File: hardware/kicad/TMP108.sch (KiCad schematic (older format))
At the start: 33 parts, among them J1 Screw_Terminal_01x08, J2 Screw_Terminal_01x08, J3 CAN, SW1 PRG, SW2 SCR, SW3 PRG-VALUE, U1 Teensy_3.2, U2 TMR-1211, U3 MCP2551-I-P

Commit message: Add smoothing capacitor to PSU
1000uF capacitor across 5V output to manage instability in ADC reference voltage.
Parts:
- added C5: 1000uF, Capacitor_THT:CP_Radial_D8.0mm_P5.00mm, symbol Device:CP
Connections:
- net +5V: now also C5.1
- net GND: now also C5.2
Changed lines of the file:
@@
 $EndComp
 Wire Wire Line
-	7900 3500 8200 3500
-Wire Wire Line
-	7900 3100 8200 3100
+	7900 3100 8000 3100
 Connection ~ 9350 3100
 Wire Wire Line
@@
 Wire Wire Line
 	900  4100 900  4550
+$Comp
+L Device:CP C5
+U 1 1 629FD333
+P 8000 3300
+F 0 "C5" H 8118 3346 50  0000 L CNN
+F 1 "1000uF" H 8000 3200 50  0000 L CNN
+F 2 "Capacitor_THT:CP_Radial_D8.0mm_P5.00mm" H 8038 3150 50  0001 C CNN
+F 3 "~" H 8000 3300 50  0001 C CNN
+	1    8000 3300
+	1    0    0    -1
+$EndComp
+Connection ~ 8000 3100
+Wire Wire Line
+	7900 3500 8000 3500
+Wire Wire Line
+	8000 3150 8000 3100
+Wire Wire Line
+	8000 3100 8200 3100
+Wire Wire Line
+	8000 3450 8000 3500
+Connection ~ 8000 3500
+Wire Wire Line
+	8000 3500 8200 3500
 $EndSCHEMATC

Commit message: Add CAN terminator
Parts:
- removed C3, C4: 560p, Capacitor_THT:C_Rect_L4.6mm_W3.0mm_P2.50mm_MKS02_FKP02, symbol Device:C
- removed R14: 100R, Resistor_THT:R_Axial_DIN0207_L6.3mm_D2.5mm_P7.62mm_Horizontal, symbol Device:R
- removed SW2: SCR, Button_Switch_THT:SW_DIP_SPSTx01_Slide_6.7x4.1mm_W7.62mm_P2.54mm_LowProfile, symbol Switch:SW_DIP_x01
- added SW2: BUS, Package_DIP:DIP-4_W7.62mm_LongPads, symbol Switch:SW_DIP_x02
- R13: value 100R -> 120R
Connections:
- net CAN_L: now also SW2.4
- net CAN_SCR: now also SW2.3
- net GND: now also SW2.2
- net TERM_A: now reaches R13.2
- net TERM_A: now also SW2.1
- no-connect marks 4 -> 7
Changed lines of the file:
@@
-$EndComp
-$Comp
-L Device:R R14
-U 1 1 5F21EFF3
-P 9000 4700
-F 0 "R14" H 8950 4700 50  0000 R CNN
-F 1 "100R" V 9000 4700 39  0000 C CNN
-F 2 "Resistor_THT:R_Axial_DIN0207_L6.3mm_D2.5mm_P7.62mm_Horizontal" V 8930 4700 50  0001 C CNN
-F 3 "~" H 9000 4700 50  0001 C CNN
-	1    9000 4700
-	-1   0    0    1
-$EndComp
-$Comp
-L Device:R R13
-U 1 1 5F21F397
-P 8750 4700
-F 0 "R13" H 8950 4700 50  0000 R CNN
-F 1 "100R" V 8750 4700 39  0000 C CNN
-F 2 "Resistor_THT:R_Axial_DIN0207_L6.3mm_D2.5mm_P7.62mm_Horizontal" V 8680 4700 50  0001 C CNN
-F 3 "~" H 8750 4700 50  0001 C CNN
-	1    8750 4700
-	1    0    0    -1
-$EndComp
-$Comp
-L Device:C C4
-U 1 1 5F233FC6
-P 9000 5000
-F 0 "C4" H 8900 5000 50  0000 R CNN
-F 1 "560p" H 9000 5100 39  0000 R CNN
-F 2 "Capacitor_THT:C_Rect_L4.6mm_W3.0mm_P2.50mm_MKS02_FKP02" H 9038 4850 50  0001 C CNN
-F 3 "~" H 9000 5000 50  0001 C CNN
-	1    9000 5000
-	-1   0    0    1
-$EndComp
-$Comp
-L Device:C C3
-U 1 1 5F2499AC
-P 8750 5000
-F 0 "C3" H 8850 5000 50  0000 L CNN
-F 1 "560p" H 8750 5100 39  0000 R CNN
-F 2 "Capacitor_THT:C_Rect_L4.6mm_W3.0mm_P2.50mm_MKS02_FKP02" H 8788 4850 50  0001 C CNN
-F 3 "~" H 8750 5000 50  0001 C CNN
-	1    8750 5000
-	-1   0    0    1
 $EndComp
 $Comp
@@
 NoConn ~ 4850 2800
 Wire Wire Line
-	8650 4300 8750 4300
-Wire Wire Line
-	8650 4500 9000 4500
-Wire Wire Line
-	8750 4550 8750 4300
-Wire Wire Line
-	9000 4550 9000 4500
-Wire Wire Line
 	7550 5150 8150 5150
 Connection ~ 7550 5150
-Wire Wire Line
-	8750 5150 9000 5150
-Connection ~ 8750 5150
 Wire Wire Line
 	7650 4600 7550 4600
@@
 	8150 4800 8150 5150
 Connection ~ 8150 4800
-Connection ~ 8150 5150
-Wire Wire Line
-	8150 5150 8750 5150
 NoConn ~ 7650 4500
 Text Label 1500 4100 0    50   ~ 0
@@
 Text Notes 10000 3800 2    50   ~ 10
 CAN INTERFACE
-Connection ~ 8750 4300
-Wire Wire Line
-	8750 4300 10200 4300
-Connection ~ 9000 4500
-Wire Wire Line
-	9000 4500 10300 4500
 Wire Notes Line
 	9100 2050 10450 2050
@@
 Text Label 4850 2700 2    50   ~ 0
 LED_PWR
-Text Label 10000 4950 2    50   ~ 0
+Text Label 10000 4950 0    50   ~ 0
 CAN_SCR
 Wire Wire Line
@@
 ADDR_7
 $Comp
-L Switch:SW_DIP_x01 SW2
-U 1 1 60541E2C
-P 1200 4100
-F 0 "SW2" H 1200 4250 50  0000 C CNN
-F 1 "SCR" H 1200 3950 50  0000 C CNN
-F 2 "Button_Switch_THT:SW_DIP_SPSTx01_Slide_6.7x4.1mm_W7.62mm_P2.54mm_LowProfile" H 1200 4100 50  0001 C CNN
-F 3 "~" H 1200 4100 50  0001 C CNN
-	1    1200 4100
-	1    0    0    -1
-$EndComp
-$Comp
 L Device:R R10
 U 1 1 6057CA79
@@
 U 1 1 60F2AB82
 P 5950 3000
-F 0 "U1" H 6500 1433 50  0000 C CNN
-F 1 "Teensy_3.2" H 6500 1524 50  0000 C CNN
+F 0 "U1" H 6100 1450 50  0000 C CNN
+F 1 "Teensy_3.2" H 6250 1550 50  0000 C CNN
 F 2 "Package_DIP:DIP-28_W15.24mm_LongPads" H 5950 3000 50  0001 C CNN
 F 3 "" H 5950 3000 50  0001 C CNN
@@
 Wire Wire Line
 	9750 3100 10400 3100
-Wire Wire Line
-	900  4100 900  4550
 $Comp
 L Device:CP C5
@@
 Wire Wire Line
 	8000 3500 8200 3500
+NoConn ~ 5400 1500
+NoConn ~ 5300 1500
+NoConn ~ 5200 1500
+$Comp
+L Device:R R13
+U 1 1 62A3BFE8
+P 9500 4650
+F 0 "R13" V 9400 4700 50  0000 R CNN
+F 1 "120R" V 9500 4650 39  0000 C CNN
+F 2 "Resistor_THT:R_Axial_DIN0207_L6.3mm_D2.5mm_P7.62mm_Horizontal" V 9430 4650 50  0001 C CNN
+F 3 "~" H 9500 4650 50  0001 C CNN
+	1    9500 4650
+	0    -1   -1   0
+$EndComp
+$Comp
+L Switch:SW_DIP_x02 SW2
+U 1 1 62A67242
+P 1200 4100
+F 0 "SW2" H 1200 4350 50  0000 C CNN
+F 1 "BUS" H 1200 3950 50  0000 C CNN
+F 2 "Package_DIP:DIP-4_W7.62mm_LongPads" H 1200 4100 50  0001 C CNN
+F 3 "~" H 1200 4100 50  0001 C CNN
+	1    1200 4100
+	1    0    0    -1
+$EndComp
+Wire Wire Line
+	900  4100 900  4550
+Text Label 10000 4650 0    50   ~ 0
+TERM_A
+Wire Wire Line
+	10000 4650 9650 4650
+Text Label 10000 4800 0    50   ~ 0
+TERM_B
+Wire Wire Line
+	8650 4300 9250 4300
+Wire Wire Line
+	9350 4650 9250 4650
+Wire Wire Line
+	9250 4650 9250 4300
+Connection ~ 9250 4300
+Wire Wire Line
+	9250 4300 10200 4300
+Wire Wire Line
+	10000 4800 9050 4800
+Wire Wire Line
+	9050 4800 9050 4500
+Connection ~ 9050 4500
+Wire Wire Line
+	9050 4500 10300 4500
+Wire Wire Line
+	8650 4500 9050 4500
+Text Label 900  4000 2    50   ~ 0
+TERM_A
+Text Label 1500 4000 0    50   ~ 0
+TERM_B
 $EndSCHEMATC

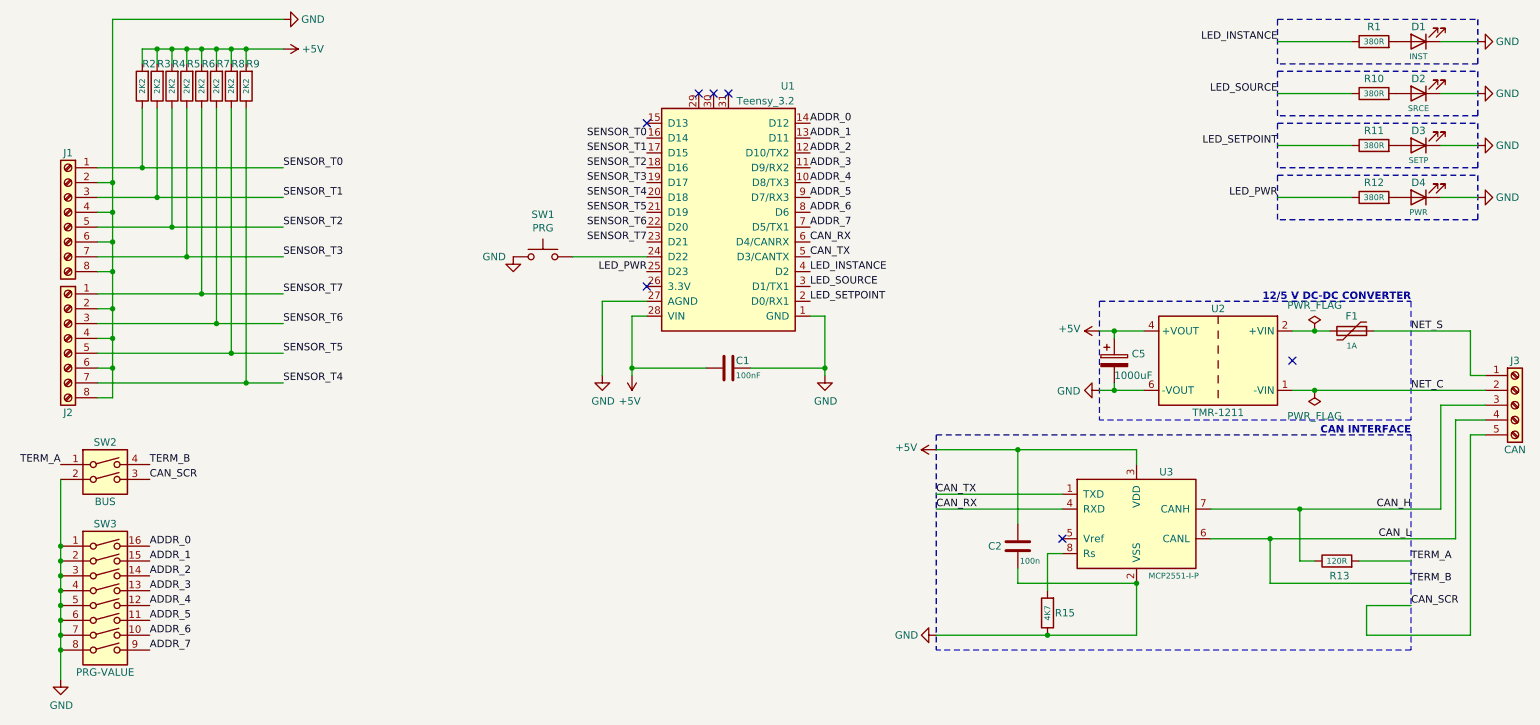
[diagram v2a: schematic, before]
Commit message: Add LED for transmit interval
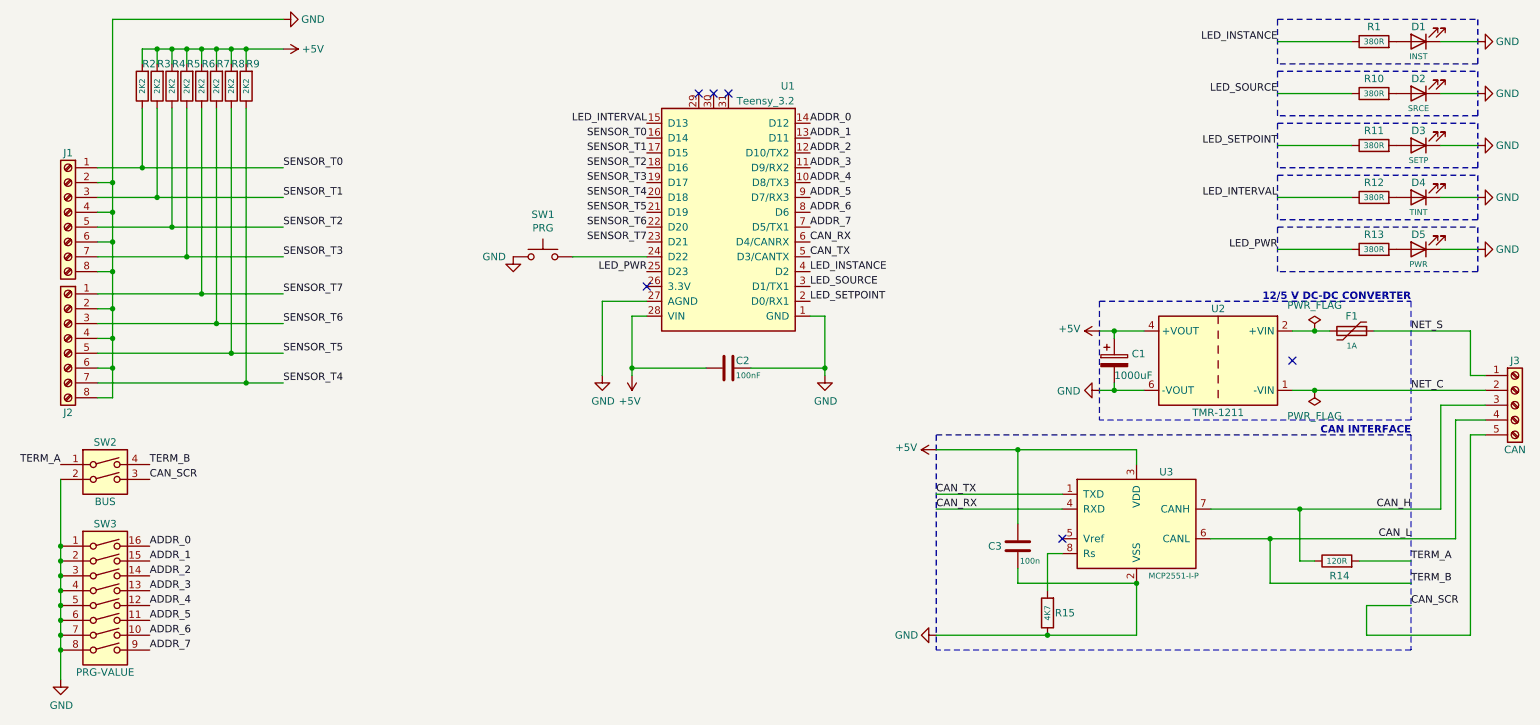
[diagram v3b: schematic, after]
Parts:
- added D4: TINT, LED_THT:LED_D1.8mm_W3.3mm_H2.4mm, symbol Device:LED
- added R12: 380R, Resistor_THT:R_Axial_DIN0207_L6.3mm_D2.5mm_P7.62mm_Horizontal, symbol Device:R
- renumbered C5 to C1, C1 to C2, C2 to C3, D4 to D5, R12 to R13, R13 to R14
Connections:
- net GND: now also D4.1 (K)
- net LED_INTERVAL: now reaches U1.15 (D13)
- net LED_INTERVAL: now also R12.1
- new net: D4.2 (A), R12.2
- no-connect marks 7 -> 6
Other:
- moved on the sheet: D5, R13
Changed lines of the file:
@@
 $EndComp
 $Comp
-L Device:R R12
+L Device:R R13
 U 1 1 5F2B75CF
-P 9750 2200
-F 0 "R12" V 9850 2200 50  0000 C CNN
-F 1 "380R" V 9750 2200 39  0000 C CNN
-F 2 "Resistor_THT:R_Axial_DIN0207_L6.3mm_D2.5mm_P7.62mm_Horizontal" V 9680 2200 50  0001 C CNN
-F 3 "~" H 9750 2200 50  0001 C CNN
-F 4 "0.125W" V 9850 2200 50  0001 C CNN "Power"
-	1    9750 2200
+P 9750 2550
+F 0 "R13" V 9850 2550 50  0000 C CNN
+F 1 "380R" V 9750 2550 39  0000 C CNN
+F 2 "Resistor_THT:R_Axial_DIN0207_L6.3mm_D2.5mm_P7.62mm_Horizontal" V 9680 2550 50  0001 C CNN
+F 3 "~" H 9750 2550 50  0001 C CNN
+F 4 "0.125W" V 9850 2550 50  0001 C CNN "Power"
+	1    9750 2550
 	0    -1   -1   0
 $EndComp
@@
 $EndComp
 $Comp
-L Device:LED D4
+L Device:LED D5
 U 1 1 5F3B6D27
-P 10050 2200
-F 0 "D4" H 10050 2100 50  0000 C CNN
-F 1 "PWR" H 10050 2300 39  0000 C CNN
-F 2 "LED_THT:LED_D3.0mm_FlatTop" H 10050 2200 50  0001 C CNN
-F 3 "https://docs.rs-online.com/0b77/0900766b814f5345.pdf" H 10050 2200 50  0001 C CNN
-	1    10050 2200
-	-1   0    0    1
-$EndComp
-$Comp
-L Device:C C2
+P 10050 2550
+F 0 "D5" H 10050 2450 50  0000 C CNN
+F 1 "PWR" H 10050 2650 39  0000 C CNN
+F 2 "LED_THT:LED_D3.0mm_FlatTop" H 10050 2550 50  0001 C CNN
+F 3 "https://docs.rs-online.com/0b77/0900766b814f5345.pdf" H 10050 2550 50  0001 C CNN
+	1    10050 2550
+	-1   0    0    1
+$EndComp
+$Comp
+L Device:C C3
 U 1 1 5F37E57C
 P 7350 4550
-F 0 "C2" H 7150 4550 50  0000 L CNN
+F 0 "C3" H 7150 4550 50  0000 L CNN
 F 1 "100n" H 7500 4450 39  0000 R CNN
 F 2 "Capacitor_THT:C_Rect_L4.6mm_W3.0mm_P2.50mm_MKS02_FKP02" H 7388 4400 50  0001 C CNN
@@
 $EndComp
 $Comp
-L Device:C C1
+L Device:C C2
 U 1 1 5F38A0E7
 P 5400 3350
-F 0 "C1" V 5450 3300 50  0000 R CNN
+F 0 "C2" V 5450 3300 50  0000 R CNN
 F 1 "100nF" V 5350 3300 39  0000 R CNN
 F 2 "Capacitor_THT:C_Rect_L4.6mm_W3.0mm_P2.50mm_MKS02_FKP02" H 5438 3200 50  0001 C CNN
@@
 Text Label 1500 4100 0    50   ~ 0
 CAN_SCR
-NoConn ~ 4850 1700
-$Comp
-L power:+5V #PWR08
+$Comp
+L power:+5V #PWR09
 U 1 1 5FC3AC81
 P 7900 3100
-F 0 "#PWR08" H 7900 2950 50  0001 C CNN
+F 0 "#PWR09" H 7900 2950 50  0001 C CNN
 F 1 "+5V" V 7915 3228 50  0000 L CNN
 F 2 "" H 7900 3100 50  0001 C CNN
@@
 $EndComp
 $Comp
-L power:GND #PWR012
+L power:GND #PWR013
 U 1 1 5FC3B74A
 P 7900 3500
-F 0 "#PWR012" H 7900 3250 50  0001 C CNN
+F 0 "#PWR013" H 7900 3250 50  0001 C CNN
 F 1 "GND" V 7905 3372 50  0000 R CNN
 F 2 "" H 7900 3500 50  0001 C CNN
@@
 $EndComp
 $Comp
-L power:+5V #PWR013
+L power:+5V #PWR014
 U 1 1 5FC442F6
 P 6800 3900
-F 0 "#PWR013" H 6800 3750 50  0001 C CNN
+F 0 "#PWR014" H 6800 3750 50  0001 C CNN
 F 1 "+5V" V 6815 4028 50  0000 L CNN
 F 2 "" H 6800 3900 50  0001 C CNN
@@
 $EndComp
 $Comp
-L power:GND #PWR014
+L power:GND #PWR015
 U 1 1 5FC44BAE
 P 6800 5150
-F 0 "#PWR014" H 6800 4900 50  0001 C CNN
+F 0 "#PWR015" H 6800 4900 50  0001 C CNN
 F 1 "GND" V 6800 4950 50  0000 C CNN
 F 2 "" H 6800 5150 50  0001 C CNN
@@
 SENSOR_T0
 $Comp
-L power:GND #PWR015
+L power:GND #PWR016
 U 1 1 6084E21C
 P 900 5450
-F 0 "#PWR015" H 900 5200 50  0001 C CNN
+F 0 "#PWR016" H 900 5200 50  0001 C CNN
 F 1 "GND" H 905 5277 50  0000 C CNN
 F 2 "" H 900 5450 50  0001 C CNN
@@
 $EndComp
 $Comp
-L power:GND #PWR09
+L power:GND #PWR010
 U 1 1 6090D237
 P 4550 3400
-F 0 "#PWR09" H 4550 3150 50  0001 C CNN
+F 0 "#PWR010" H 4550 3150 50  0001 C CNN
 F 1 "GND" H 4555 3227 50  0000 C CNN
 F 2 "" H 4550 3400 50  0001 C CNN
@@
 $EndComp
 $Comp
-L power:+5V #PWR010
+L power:+5V #PWR011
 U 1 1 6090DC41
 P 4750 3400
-F 0 "#PWR010" H 4750 3250 50  0001 C CNN
+F 0 "#PWR011" H 4750 3250 50  0001 C CNN
 F 1 "+5V" H 4765 3573 50  0000 C CNN
 F 2 "" H 4750 3400 50  0001 C CNN
@@
 Connection ~ 4750 3350
 $Comp
-L power:GND #PWR011
+L power:GND #PWR012
 U 1 1 6096FBD9
 P 6050 3400
-F 0 "#PWR011" H 6050 3150 50  0001 C CNN
+F 0 "#PWR012" H 6050 3150 50  0001 C CNN
 F 1 "GND" H 6055 3227 50  0000 C CNN
 F 2 "" H 6050 3400 50  0001 C CNN
@@
 CAN INTERFACE
 Wire Notes Line
-	9100 2050 10450 2050
-Wire Notes Line
-	10450 2050 10450 2350
-Wire Notes Line
-	10450 2350 9100 2350
-Wire Notes Line
-	9100 2350 9100 2050
-Text Label 9100 2200 2    50   ~ 0
+	9100 2400 10450 2400
+Wire Notes Line
+	10450 2400 10450 2700
+Wire Notes Line
+	10450 2700 9100 2700
+Wire Notes Line
+	9100 2700 9100 2400
+Text Label 9100 2550 2    50   ~ 0
 LED_PWR
 Wire Wire Line
-	9100 2200 9600 2200
-Wire Wire Line
-	10200 2200 10450 2200
-$Comp
-L power:GND #PWR06
+	9100 2550 9600 2550
+Wire Wire Line
+	10200 2550 10450 2550
+$Comp
+L power:GND #PWR07
 U 1 1 5FFE90AB
-P 10450 2200
-F 0 "#PWR06" H 10450 1950 50  0001 C CNN
-F 1 "GND" V 10450 2000 50  0000 C CNN
-F 2 "" H 10450 2200 50  0001 C CNN
-F 3 "" H 10450 2200 50  0001 C CNN
-	1    10450 2200
+P 10450 2550
+F 0 "#PWR07" H 10450 2300 50  0001 C CNN
+F 1 "GND" V 10450 2350 50  0000 C CNN
+F 2 "" H 10450 2550 50  0001 C CNN
+F 3 "" H 10450 2550 50  0001 C CNN
+	1    10450 2550
 	0    -1   -1   0
 $EndComp
@@
 $EndComp
 $Comp
-L power:GND #PWR07
+L power:GND #PWR08
 U 1 1 6058F22D
 P 3950 2600
-F 0 "#PWR07" H 3950 2350 50  0001 C CNN
+F 0 "#PWR08" H 3950 2350 50  0001 C CNN
 F 1 "GND" H 3900 2600 50  0000 R CNN
 F 2 "" H 3950 2600 50  0001 C CNN
@@
 	9750 3100 10400 3100
 $Comp
-L Device:CP C5
+L Device:CP C1
 U 1 1 629FD333
 P 8000 3300
-F 0 "C5" H 8118 3346 50  0000 L CNN
+F 0 "C1" H 8118 3346 50  0000 L CNN
 F 1 "1000uF" H 8000 3200 50  0000 L CNN
 F 2 "Capacitor_THT:CP_Radial_D8.0mm_P5.00mm" H 8038 3150 50  0001 C CNN
@@
 NoConn ~ 5200 1500
 $Comp
-L Device:R R13
+L Device:R R14
 U 1 1 62A3BFE8
 P 9500 4650
-F 0 "R13" V 9400 4700 50  0000 R CNN
+F 0 "R14" V 9400 4700 50  0000 R CNN
 F 1 "120R" V 9500 4650 39  0000 C CNN
 F 2 "Resistor_THT:R_Axial_DIN0207_L6.3mm_D2.5mm_P7.62mm_Horizontal" V 9430 4650 50  0001 C CNN
@@
 Text Label 1500 4000 0    50   ~ 0
 TERM_B
+Text Label 4850 1700 2    50   ~ 0
+LED_INTERVAL
+$Comp
+L Device:R R12
+U 1 1 62A88292
+P 9750 2200
+F 0 "R12" V 9850 2200 50  0000 C CNN
+F 1 "380R" V 9750 2200 39  0000 C CNN
+F 2 "Resistor_THT:R_Axial_DIN0207_L6.3mm_D2.5mm_P7.62mm_Horizontal" V 9680 2200 50  0001 C CNN
+F 3 "~" H 9750 2200 50  0001 C CNN
+F 4 "0.125W" V 9850 2200 50  0001 C CNN "Power"
+	1    9750 2200
+	0    -1   -1   0
+$EndComp
+$Comp
+L Device:LED D4
+U 1 1 62A8856C
+P 10050 2200
+F 0 "D4" H 10050 2100 50  0000 C CNN
+F 1 "TINT" H 10050 2300 39  0000 C CNN
+F 2 "LED_THT:LED_D1.8mm_W3.3mm_H2.4mm" H 10050 2200 50  0001 C CNN
+F 3 "https://docs.rs-online.com/0b77/0900766b814f5345.pdf" H 10050 2200 50  0001 C CNN
+	1    10050 2200
+	-1   0    0    1
+$EndComp
+Wire Notes Line
+	9100 2050 10450 2050
+Wire Notes Line
+	10450 2050 10450 2350
+Wire Notes Line
+	10450 2350 9100 2350
+Wire Notes Line
+	9100 2350 9100 2050
+Text Label 9100 2200 2    50   ~ 0
+LED_INTERVAL
+Wire Wire Line
+	9100 2200 9600 2200
+Wire Wire Line
+	10200 2200 10450 2200
+$Comp
+L power:GND #PWR06
+U 1 1 62A8857D
+P 10450 2200
+F 0 "#PWR06" H 10450 1950 50  0001 C CNN
+F 1 "GND" V 10450 2000 50  0000 C CNN
+F 2 "" H 10450 2200 50  0001 C CNN
+F 3 "" H 10450 2200 50  0001 C CNN
+	1    10450 2200
+	0    -1   -1   0
+$EndComp
 $EndSCHEMATC
